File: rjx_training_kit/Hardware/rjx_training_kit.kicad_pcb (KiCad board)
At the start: 2 copper layers, 107 parts, among them J1 Barrel_Jack_Switch, J2 Conn_01x32_Pin, J3 Conn_01x32_Pin, J4 LiPo_4.2V, J5 LiPo_4.2V, J6 CHG_OUT, J7 CAN_Bus, J8 CAN_Bus, Q1 BC817, Q2 BC817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

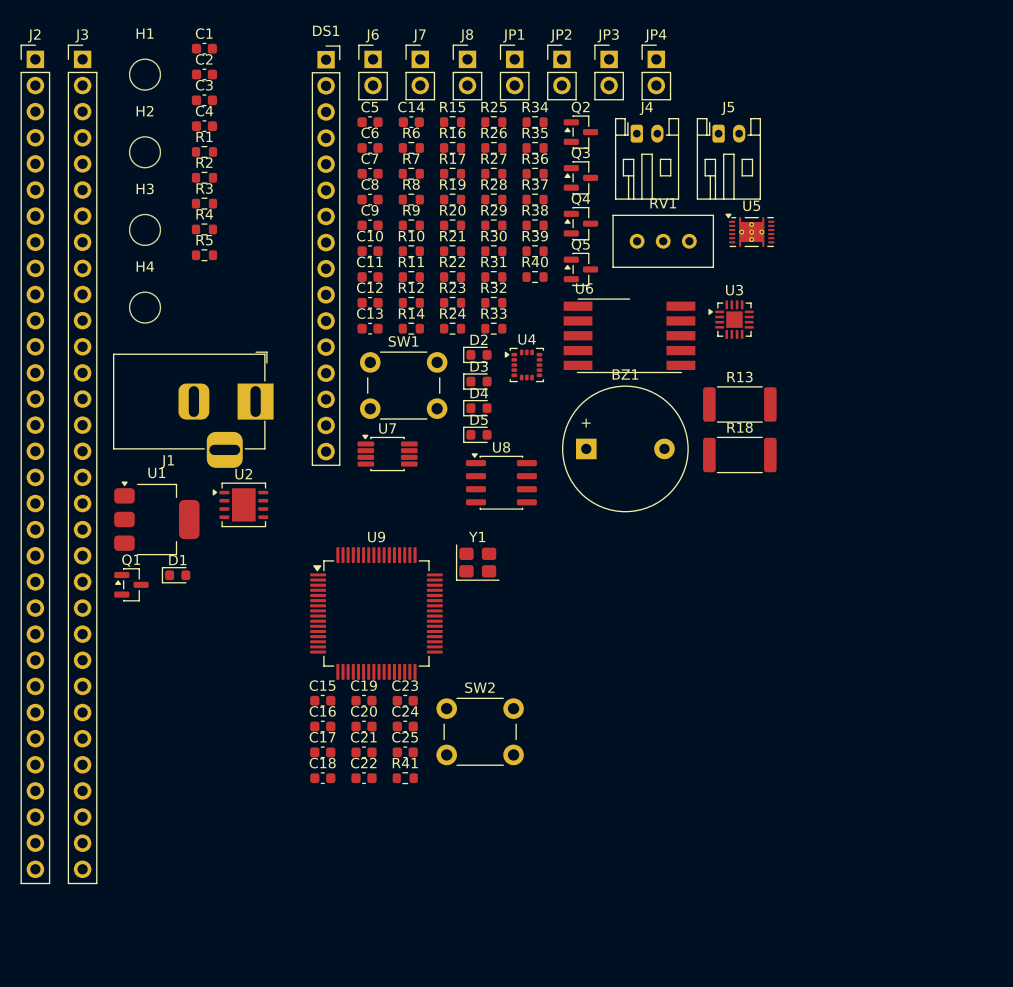
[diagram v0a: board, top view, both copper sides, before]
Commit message: [RJX]: Deleted netlist because it is poor for version control. The PCB is directly updated from the schematic instead of relying on netlists.
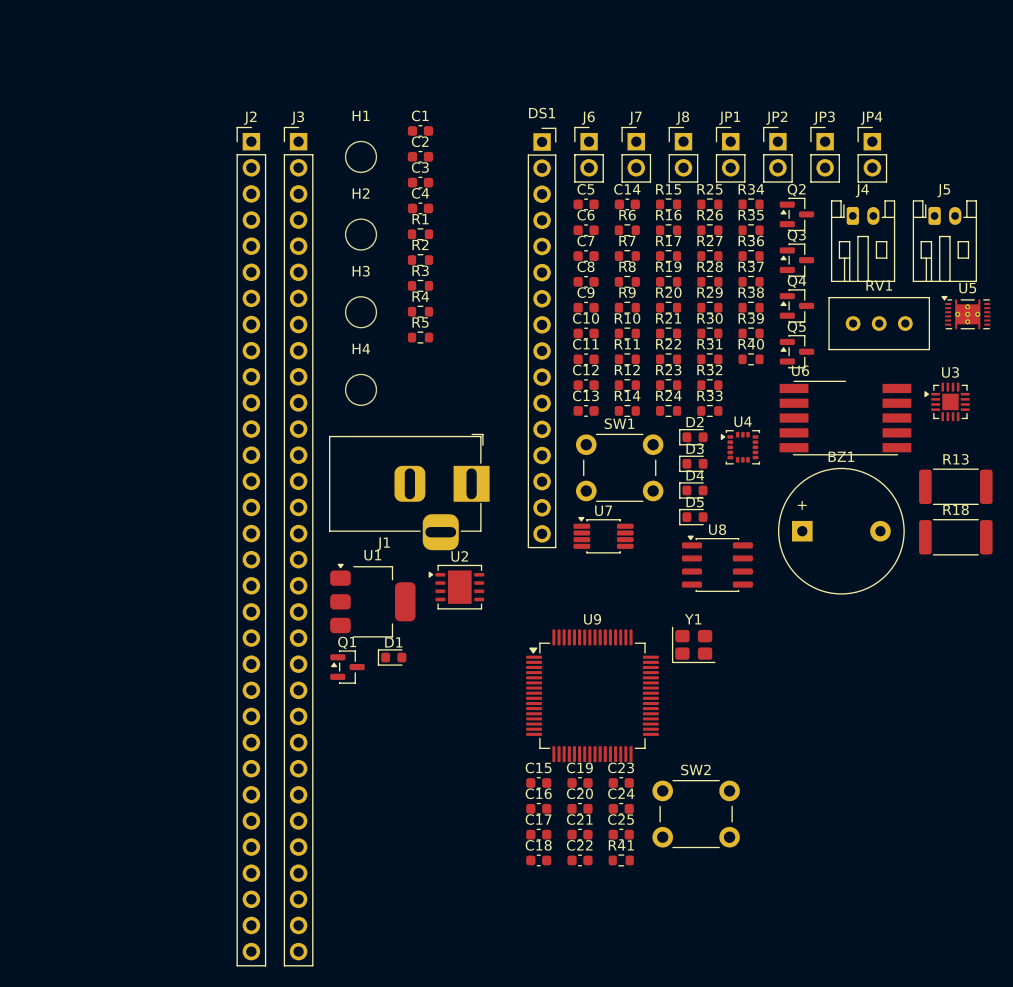
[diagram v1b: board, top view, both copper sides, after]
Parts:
- moved J4 22.5 mm to (147.0, 65.8)
- moved D2 22.5 mm to (131.7, 87.3)
- moved D3 22.5 mm to (131.7, 89.9)
- moved D4 22.5 mm to (131.7, 92.5)
- moved D5 22.5 mm to (131.7, 95.0)
- moved JP1 22.5 mm to (135.1, 58.5)
- moved JP2 22.5 mm to (139.7, 58.5)
- moved U4 22.5 mm to (136.3, 88.2)
- moved C6 22.5 mm to (121.1, 67.2)
- moved J5 22.5 mm to (155.0, 65.8)
- moved R1 22.5 mm to (105.0, 67.5)
- moved R26 22.5 mm to (133.1, 67.2)
- moved R35 22.5 mm to (137.1, 67.2)
- moved R6 22.5 mm to (125.1, 67.2)
- moved C1 22.5 mm to (105.0, 57.5)
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
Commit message: [RJX]: Board setup + place and route in progress.
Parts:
- C23, C24, C25: moved to B.Cu
- moved Q2 164.5 mm to (20.5, 177.0)
- moved C14 158.7 mm to (257.2, 152.5)
- moved C13 156.0 mm to (258.2, 159.0)
- moved R7 155.8 mm to (18.2, 183.0)
- moved R36 153.9 mm to (266.2, 153.6)
- moved J7 153.9 mm to (255.0, 142.5)
- moved J8 153.9 mm to (259.6, 142.5)
- moved U8 151.8 mm to (274.0, 158.1)
- moved BZ1 151.0 mm to (22.4, 188.5)
- moved JP3 148.6 mm to (268.0, 141.0)
- moved C6 143.7 mm to (261.0, 34.3)
- moved C11 143.0 mm to (260.2, 46.5)
- moved R10 143.0 mm to (264.2, 44.0)
- moved R11 143.0 mm to (264.2, 46.5)
- moved R20 143.0 mm to (268.2, 41.5)
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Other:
- board outline added: 100 x 100 mm
- copper layers 2 -> 4

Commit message: [RJX]: Component placement in progress.
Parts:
- added J9: Conn_01x03_Pin, Connector_PinHeader_2.54mm:PinHeader_1x03_P2.54mm_Horizontal, F.Cu at (134.0, 58.4)
- C23, C24, C25: moved to F.Cu
- moved D5 174.7 mm to (75.6, 79.4)
- moved R32 173.0 mm to (75.6, 76.2)
- moved R33 171.2 mm to (75.6, 82.5)
- moved U5 166.5 mm to (108.0, 76.9)
- moved R10 163.2 mm to (104.0, 74.9), turned to 180 degrees
- moved C6 159.9 mm to (108.0, 80.6)
- moved R20 159.5 mm to (112.2, 74.9), turned to 180 degrees
- moved C11 159.4 mm to (104.0, 78.1), turned to 180 degrees
- moved R11 155.2 mm to (112.2, 78.1), turned to 180 degrees
- moved R31 108.3 mm to (67.9, 87.0)
- moved SW1 98.8 mm to (73.0, 86.9)
- moved U1 19.7 mm to (54.6, 69.2), turned to 90 degrees
- moved C2 14.1 mm to (54.0, 76.2), turned to 180 degrees
- moved C1 9.84 mm to (57.8, 76.2), turned to 0 degrees
- moved C15 9.54 mm to (70.5, 76.2), turned to 180 degrees
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
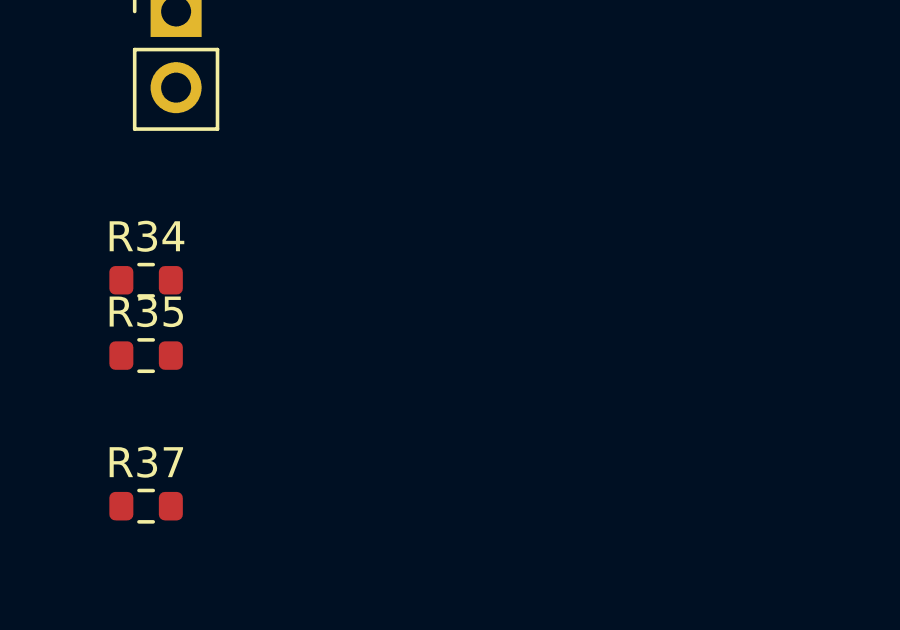
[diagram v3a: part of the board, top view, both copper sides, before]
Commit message: [RJX]: Modified the schematic to account for different types of LCDs (some have current-limiting resistors, others don't). Also changed Links.md to an inner README.md file
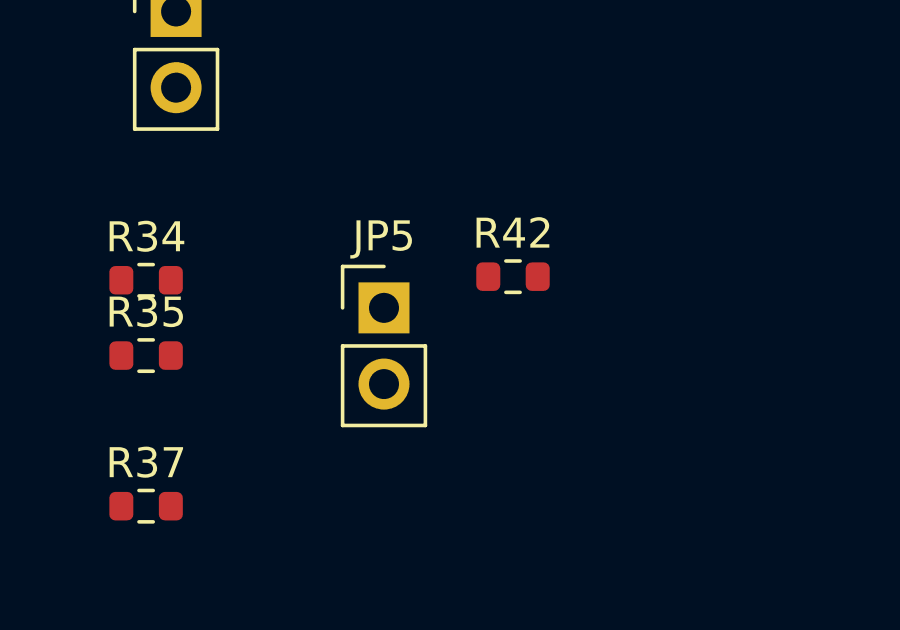
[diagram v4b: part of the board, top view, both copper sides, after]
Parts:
- added JP5: Jumper_2_Open, Connector_PinHeader_2.54mm:PinHeader_1x02_P2.54mm_Vertical, F.Cu at (180.9, 51.8)
- added R42: 300, Resistor_SMD:R_0603_1608Metric, F.Cu at (185.2, 50.8)

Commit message: [RJX]: Component placement nearing completion. Though it's still subject to change after DRC is performed
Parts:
- moved U8 192.0 mm to (89.5, 104.8), turned to -90 degrees
- moved C13 180.6 mm to (87.6, 99.7), turned to 180 degrees
- moved R36 180.1 mm to (90.2, 115.1), turned to 90 degrees
- moved C14 176.7 mm to (85.7, 109.9), turned to 180 degrees
- moved JP3 176.4 mm to (93.3, 116.2), turned to 180 degrees
- moved R38 174.6 mm to (101.6, 77.5)
- moved R40 174.0 mm to (101.6, 80.6)
- moved R39 172.9 mm to (101.6, 74.3)
- moved J7 171.7 mm to (85.7, 113.7)
- moved J8 164.3 mm to (97.8, 113.7)
- moved U7 137.2 mm to (108.0, 78.1)
- moved C12 133.7 mm to (113.7, 76.8)
- moved JP5 128.9 mm to (52.1, 48.3), turned to 180 degrees
- moved JP4 127.2 mm to (47.0, 48.3), turned to 180 degrees
- moved R34 115.2 mm to (57.8, 50.0), turned to 90 degrees
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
